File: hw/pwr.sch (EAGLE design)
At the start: 27 parts, among them IC1 MAX640, IC2 MAX640, IC3 MAX640

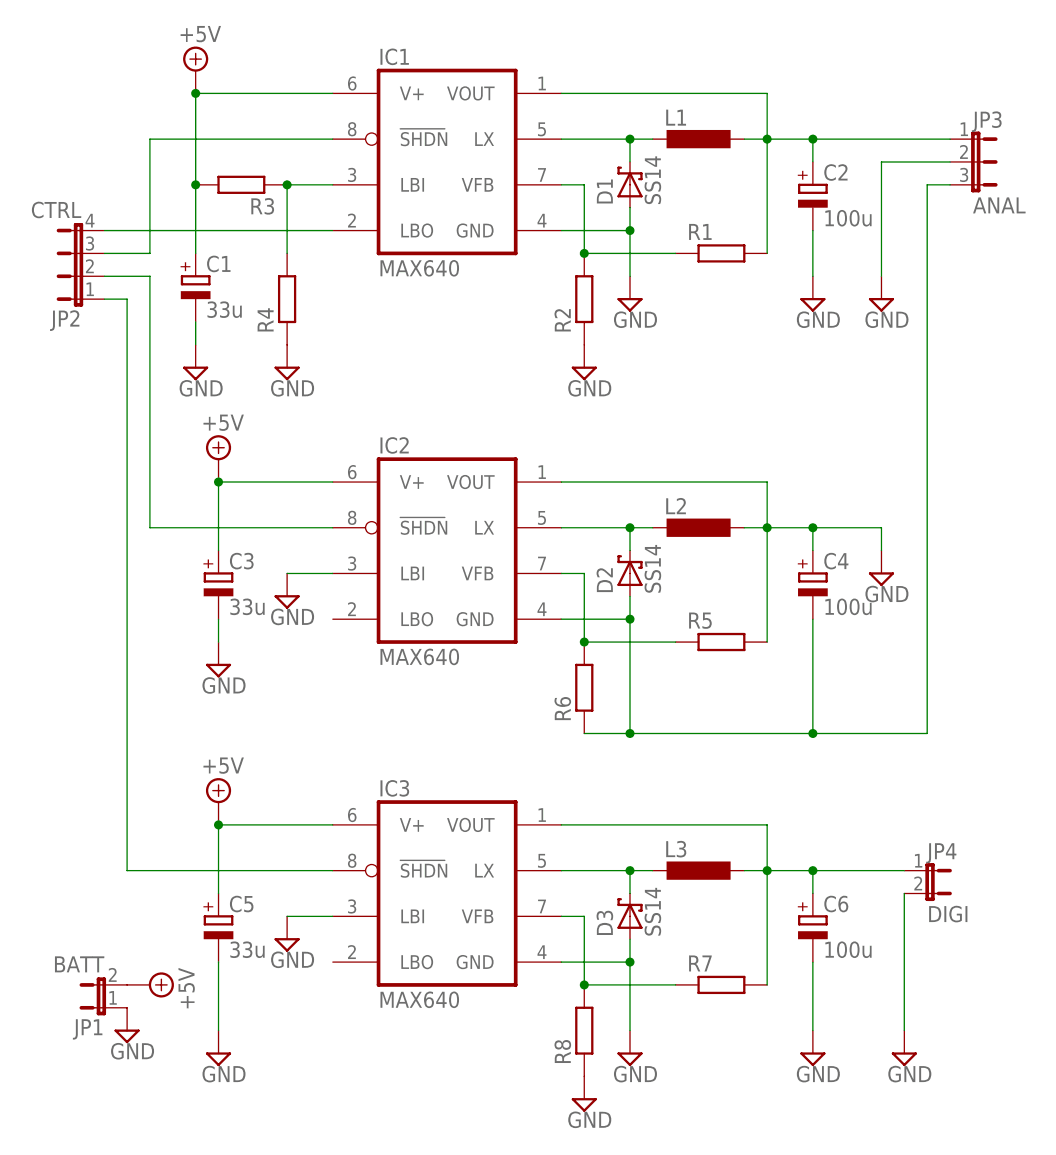
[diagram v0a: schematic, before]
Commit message: created power board
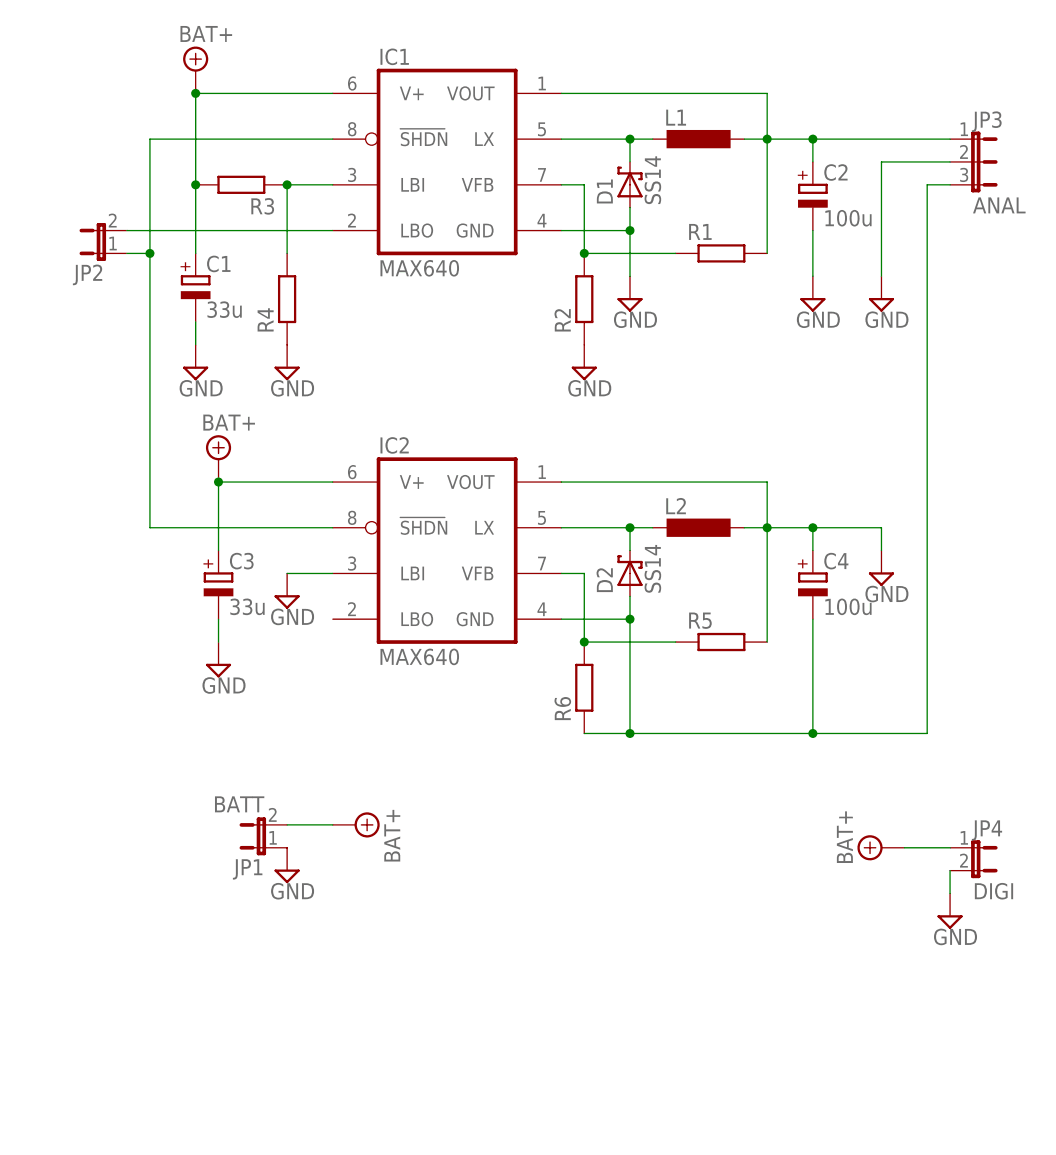
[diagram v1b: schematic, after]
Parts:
- removed C5: 33u, rcl:CPOL-EUSMCC
- removed C6: 100u, rcl:CPOL-EUSMCC
- removed D3: SS14, mindspy:SS14
- removed IC3: MAX640, mindspy:MAX640
- removed L3: (no value), rcl:L-EUL1812
- removed R7, R8: (no value), rcl:R-EU_R1206
- JP2: value CTRL -> (none); device jumper:JP4E -> jumper:JP1E
- R1, R2, R3, R4, R5, R6: device rcl:R-EU_R1206 -> rcl:R-EU_R0805
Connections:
- removed net +5V: C1.+, C3.+, C5.+, IC1.V+, IC2.V+, IC3.V+, JP1.2, R3.2
- removed net 3V3: C6.+, IC3.VOUT, JP4.1, L3.1, R7.2
- removed net N$11: IC2.SHDN, JP2.2
- removed net N$13: IC3.VFB, R7.1, R8.2
- removed net N$14: IC3.SHDN, JP2.1
- removed net N$2: IC1.SHDN, JP2.3
- removed net N$3: IC1.LBO, JP2.4
- removed net N$9: D3.C, IC3.LX, L3.2
- new net LBO: IC1.LBO, JP2.2
- new net SHDN: IC1.SHDN, IC2.SHDN, JP2.1
- new net VBAT: C1.+, C3.+, IC1.V+, IC2.V+, JP1.2, JP4.1, R3.2
- net GND: no longer C5.-, C6.-, D3.A, IC3.GND, IC3.LBI, R8.1
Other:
- moved on the sheet: JP1, JP4

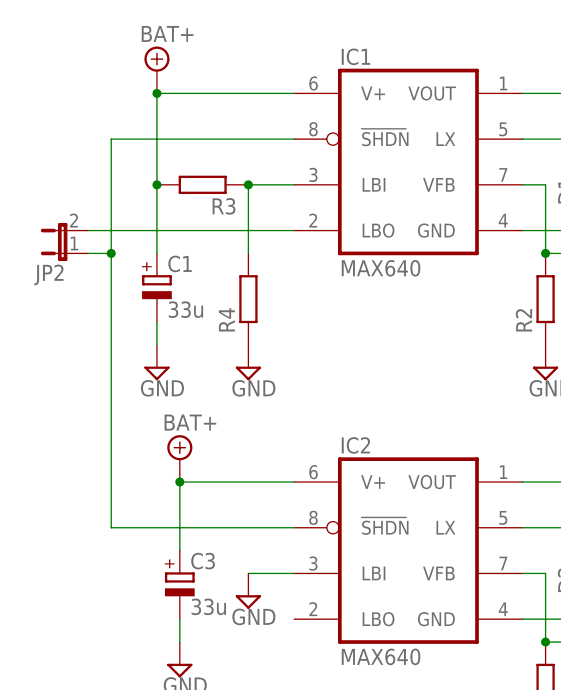
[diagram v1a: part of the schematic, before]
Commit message: Fix problems with polarity and route length and crossing  as well
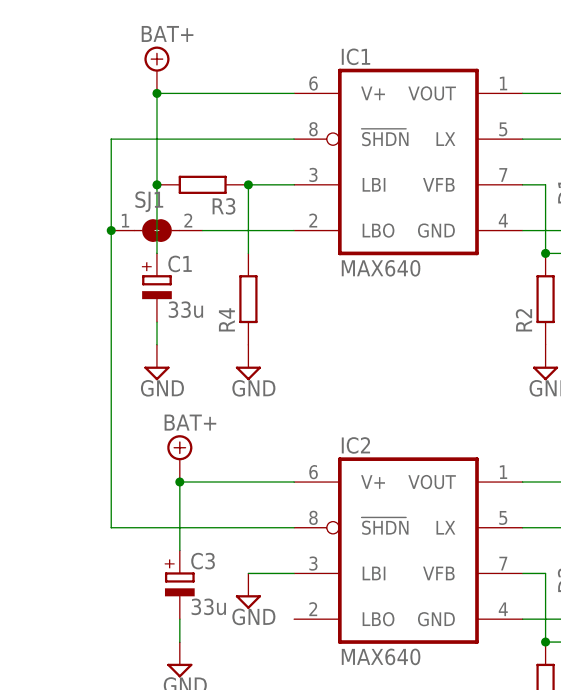
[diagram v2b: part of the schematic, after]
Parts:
- removed JP2: (no value), jumper:JP1E
- added SJ1: (no value), jumper:SJ
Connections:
- net LBO: now also SJ1.2; no longer JP2.2
- net SHDN: now also SJ1.1; no longer JP2.1
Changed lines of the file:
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@@
 <part name="JP4" library="jumper" deviceset="JP1E" device="" value="DIGI"/>
 <part name="SUPPLY15" library="supply2" deviceset="+5V" device="" value="BAT+"/>
-<part name="JP2" library="jumper" deviceset="JP1E" device=""/>
+<part name="SJ1" library="jumper" deviceset="SJ" device=""/>
 </parts>
 <sheets>
@@
 <instance part="JP4" gate="A" x="88.9" y="-7.62" rot="R270"/>
 <instance part="SUPPLY15" gate="+5V" x="78.74" y="-7.62" rot="R90"/>
-<instance part="JP2" gate="A" x="-7.62" y="58.42" rot="R90"/>
+<instance part="SJ1" gate="1" x="2.54" y="60.96"/>
 </instances>
 <busses>
@@
 <net name="SHDN" class="0">
 <segment>
-<wire x1="-2.54" y1="58.42" x2="-2.54" y2="27.94" width="0.1524" layer="91"/>
+<wire x1="-2.54" y1="60.96" x2="-2.54" y2="27.94" width="0.1524" layer="91"/>
 <pinref part="IC2" gate="G$1" pin="SHDN"/>
 <wire x1="17.78" y1="27.94" x2="-2.54" y2="27.94" width="0.1524" layer="91"/>
-<wire x1="-2.54" y1="71.12" x2="-2.54" y2="58.42" width="0.1524" layer="91"/>
-<wire x1="-2.54" y1="58.42" x2="-5.08" y2="58.42" width="0.1524" layer="91"/>
+<wire x1="-2.54" y1="71.12" x2="-2.54" y2="60.96" width="0.1524" layer="91"/>
 <pinref part="IC1" gate="G$1" pin="SHDN"/>
 <wire x1="17.78" y1="71.12" x2="-2.54" y2="71.12" width="0.1524" layer="91"/>
-<pinref part="JP2" gate="A" pin="1"/>
-<junction x="-2.54" y="58.42"/>
+<pinref part="SJ1" gate="1" pin="1"/>
+<junction x="-2.54" y="60.96"/>
 </segment>
 </net>
@@
 <segment>
 <pinref part="IC1" gate="G$1" pin="LBO"/>
-<wire x1="17.78" y1="60.96" x2="-5.08" y2="60.96" width="0.1524" layer="91"/>
-<pinref part="JP2" gate="A" pin="2"/>
-</segment>
-</net>
+<wire x1="17.78" y1="60.96" x2="7.62" y2="60.96" width="0.1524" layer="91"/>
+<pinref part="SJ1" gate="1" pin="2"/>
+</segment>
+</net>

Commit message: Sargon rocks
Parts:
- removed SJ1: (no value), jumper:SJ
- L1, L2: device rcl:L-EUL1812 -> rcl:L-EUWE-TPC
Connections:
- removed net LBO: IC1.LBO, SJ1.2
- net SHDN: no longer SJ1.1
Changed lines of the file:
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@@
 <grid distance="0.1" unitdist="inch" unit="inch" style="lines" multiple="1" display="no" altdistance="0.01" altunitdist="inch" altunit="inch"/>
 <layers>
-<layer number="1" name="Top" color="4" fill="1" visible="no" active="no"/>
-<layer number="16" name="Bottom" color="1" fill="1" visible="no" active="no"/>
-<layer number="17" name="Pads" color="2" fill="1" visible="no" active="no"/>
-<layer number="18" name="Vias" color="2" fill="1" visible="no" active="no"/>
-<layer number="19" name="Unrouted" color="6" fill="1" visible="no" active="no"/>
-<layer number="20" name="Dimension" color="15" fill="1" visible="no" active="no"/>
-<layer number="21" name="tPlace" color="7" fill="1" visible="no" active="no"/>
-<layer number="22" name="bPlace" color="7" fill="1" visible="no" active="no"/>
-<layer number="23" name="tOrigins" color="15" fill="1" visible="no" active="no"/>
-<layer number="24" name="bOrigins" color="15" fill="1" visible="no" active="no"/>
-<layer number="25" name="tNames" color="7" fill="1" visible="no" active="no"/>
-<layer number="26" name="bNames" color="7" fill="1" visible="no" active="no"/>
-<layer number="27" name="tValues" color="7" fill="1" visible="no" active="no"/>
-<layer number="28" name="bValues" color="7" fill="1" visible="no" active="no"/>
+<layer number="1" name="Top" color="4" fill="1" visible="yes" active="no"/>
+<layer number="16" name="Bottom" color="1" fill="1" visible="yes" active="no"/>
+<layer number="17" name="Pads" color="2" fill="1" visible="yes" active="no"/>
+<layer number="18" name="Vias" color="2" fill="1" visible="yes" active="no"/>
+<layer number="19" name="Unrouted" color="6" fill="1" visible="yes" active="no"/>
+<layer number="20" name="Dimension" color="15" fill="1" visible="yes" active="no"/>
+<layer number="21" name="tPlace" color="7" fill="1" visible="yes" active="no"/>
+<layer number="22" name="bPlace" color="7" fill="1" visible="yes" active="no"/>
+<layer number="23" name="tOrigins" color="15" fill="1" visible="yes" active="no"/>
+<layer number="24" name="bOrigins" color="15" fill="1" visible="yes" active="no"/>
+<layer number="25" name="tNames" color="7" fill="1" visible="yes" active="no"/>
+<layer number="26" name="bNames" color="7" fill="1" visible="yes" active="no"/>
+<layer number="27" name="tValues" color="7" fill="1" visible="yes" active="no"/>
+<layer number="28" name="bValues" color="7" fill="1" visible="yes" active="no"/>
 <layer number="29" name="tStop" color="7" fill="3" visible="no" active="no"/>
 <layer number="30" name="bStop" color="7" fill="6" visible="no" active="no"/>
@@
 <layer number="35" name="tGlue" color="7" fill="4" visible="no" active="no"/>
 <layer number="36" name="bGlue" color="7" fill="5" visible="no" active="no"/>
-<layer number="37" name="tTest" color="7" fill="1" visible="no" active="no"/>
-<layer number="38" name="bTest" color="7" fill="1" visible="no" active="no"/>
+<layer number="37" name="tTest" color="7" fill="1" visible="yes" active="no"/>
+<layer number="38" name="bTest" color="7" fill="1" visible="yes" active="no"/>
 <layer number="39" name="tKeepout" color="4" fill="11" visible="no" active="no"/>
 <layer number="40" name="bKeepout" color="1" fill="11" visible="no" active="no"/>
@@
 <layer number="44" name="Drills" color="7" fill="1" visible="no" active="no"/>
 <layer number="45" name="Holes" color="7" fill="1" visible="no" active="no"/>
-<layer number="46" name="Milling" color="3" fill="1" visible="no" active="no"/>
-<layer number="47" name="Measures" color="7" fill="1" visible="no" active="no"/>
-<layer number="48" name="Document" color="7" fill="1" visible="no" active="no"/>
-<layer number="49" name="Reference" color="7" fill="1" visible="no" active="no"/>
-<layer number="51" name="tDocu" color="7" fill="1" visible="no" active="no"/>
-<layer number="52" name="bDocu" color="7" fill="1" visible="no" active="no"/>
+<layer number="46" name="Milling" color="3" fill="1" visible="yes" active="no"/>
+<layer number="47" name="Measures" color="7" fill="1" visible="yes" active="no"/>
+<layer number="48" name="Document" color="7" fill="1" visible="yes" active="no"/>
+<layer number="49" name="Reference" color="7" fill="1" visible="yes" active="no"/>
+<layer number="51" name="tDocu" color="7" fill="1" visible="yes" active="no"/>
+<layer number="52" name="bDocu" color="7" fill="1" visible="yes" active="no"/>
 <layer number="91" name="Nets" color="2" fill="1" visible="yes" active="yes"/>
 <layer number="92" name="Busses" color="1" fill="1" visible="yes" active="yes"/>
@@
 <parts>
 <part name="IC1" library="mindspy" deviceset="MAX640" device=""/>
-<part name="L1" library="rcl" deviceset="L-EU" device="L1812"/>
+<part name="L1" library="rcl" deviceset="L-EU" device="WE-TPC"/>
 <part name="D1" library="mindspy" deviceset="SS14" device=""/>
 <part name="C1" library="rcl" deviceset="CPOL-EU" device="SMCC" value="33u"/>
@@
 <part name="SUPPLY8" library="supply2" deviceset="GND" device=""/>
 <part name="IC2" library="mindspy" deviceset="MAX640" device=""/>
-<part name="L2" library="rcl" deviceset="L-EU" device="L1812"/>
+<part name="L2" library="rcl" deviceset="L-EU" device="WE-TPC"/>
 <part name="D2" library="mindspy" deviceset="SS14" device=""/>
 <part name="C3" library="rcl" deviceset="CPOL-EU" device="SMCC" value="33u"/>
@@
 <part name="JP4" library="jumper" deviceset="JP1E" device="" value="DIGI"/>
 <part name="SUPPLY15" library="supply2" deviceset="+5V" device="" value="BAT+"/>
-<part name="SJ1" library="jumper" deviceset="SJ" device=""/>
 </parts>
 <sheets>
@@
 <instance part="JP4" gate="A" x="88.9" y="-7.62" rot="R270"/>
 <instance part="SUPPLY15" gate="+5V" x="78.74" y="-7.62" rot="R90"/>
-<instance part="SJ1" gate="1" x="2.54" y="60.96"/>
 </instances>
 <busses>
@@
 <net name="SHDN" class="0">
 <segment>
-<wire x1="-2.54" y1="60.96" x2="-2.54" y2="27.94" width="0.1524" layer="91"/>
+<wire x1="-2.54" y1="71.12" x2="-2.54" y2="27.94" width="0.1524" layer="91"/>
 <pinref part="IC2" gate="G$1" pin="SHDN"/>
 <wire x1="17.78" y1="27.94" x2="-2.54" y2="27.94" width="0.1524" layer="91"/>
-<wire x1="-2.54" y1="71.12" x2="-2.54" y2="60.96" width="0.1524" layer="91"/>
 <pinref part="IC1" gate="G$1" pin="SHDN"/>
 <wire x1="17.78" y1="71.12" x2="-2.54" y2="71.12" width="0.1524" layer="91"/>
-<pinref part="SJ1" gate="1" pin="1"/>
-<junction x="-2.54" y="60.96"/>
 </segment>
 </net>
@@
 </segment>
 </net>
-<net name="LBO" class="0">
-<segment>
-<pinref part="IC1" gate="G$1" pin="LBO"/>
-<wire x1="17.78" y1="60.96" x2="7.62" y2="60.96" width="0.1524" layer="91"/>
-<pinref part="SJ1" gate="1" pin="2"/>
-</segment>
-</net>
